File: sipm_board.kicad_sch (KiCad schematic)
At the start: 15 parts, among them Q3 MMBT5088LT1G, Q4 MMBT5088LT1G, U10 MICROFC-60035-SMT-TR1, U9 TPS7B6950DBVR

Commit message: C17,C19,FB1,FB2,FB3 footprint fix
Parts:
- C17, C19: footprint CL21A475KBQNNNE:CAPC2012X140N -> Capacitor_SMD:C_0603_1608Metric; Availability In Stock -> (none); Check_prices https://www.snapeda.com/parts/CL21A475KBQNNNE/Samsung/view-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 -> https://www.snapeda.com/parts/CL10A225KB8NNNC/Samsung%20Ele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; Description_1 CL21 Series 4.7 uF 50 V ±10 % Tolerance X5R SMT Multilayer 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 -> Multilayer Ceramic Capacitors MLCC - SMD/SMT 2.2uF+/-10% 50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; Package 0805 Samsung -> 0603; SnapEDA_Link https://www.snapeda.com/parts/CL21A475KBQNNNE/Samsung/view-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 -> https://www.snapeda.com/parts/CL10A225KB8NNNC/Samsung%20Ele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
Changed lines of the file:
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@@
+	)
+	(symbol
+		(lib_id "CL21A475KBQNNNE:CL21A475KBQNNNE")
+		(at 146.05 101.6 90)
+		(unit 1)
+		(exclude_from_sim no)
+		(in_bom yes)
+		(on_board yes)
+		(dnp no)
+		(property "Reference" "C19"
+			(at 139.7 98.552 90)
+			(effects
+				(font
+					(size 1.27 1.27)
+				)
+				(justify right)
+			)
+		)
+		(property "Value" "2.2u"
+			(at 139.7 101.092 90)
+			(effects
+				(font
+					(size 1.27 1.27)
+				)
+				(justify right)
+			)
+		)
+		(property "Footprint" "Capacitor_SMD:C_0603_1608Metric"
+			(at 146.05 101.6 0)
+			(effects
+				(font
+					(size 1.27 1.27)
+				)
+				(justify bottom)
+				(hide yes)
+			)
+		)
+		(property "Datasheet" ""
+			(at 146.05 101.6 0)
+			(effects
+				(font
+					(size 1.27 1.27)
+				)
+				(hide yes)
+			)
+		)
+		(property "Description" ""
+			(at 146.05 101.6 0)
+			(effects
+				(font
+					(size 1.27 1.27)
+				)
+				(hide yes)
+			)
+		)
+		(property "MF" "Samsung Electro-Mechanics"
+			(at 146.05 101.6 0)
+			(effects
+				(font
+					(size 1.27 1.27)
+				)
+				(justify bottom)
+				(hide yes)
+			)
+		)
+		(property "Description_1" "Multilayer Ceramic Capacitors MLCC - SMD/SMT 2.2uF+/-10% 50V X5R 1608 "
+			(at 146.05 101.6 0)
+			(effects
+				(font
+					(size 1.27 1.27)
+				)
+				(justify bottom)
+				(hide yes)
+			)
+		)
+		(property "Package" "0603"
+			(at 146.05 101.6 0)
+			(effects
+				(font
+					(size 1.27 1.27)
+				)
+				(justify bottom)
+				(hide yes)
+			)
+		)
+		(property "Price" "None"
+			(at 146.05 101.6 0)
+			(effects
+				(font
+					(size 1.27 1.27)
+				)
+				(justify bottom)
+				(hide yes)
+			)
+		)
+		(property "SnapEDA_Link" "https://www.snapeda.com/parts/CL10A225KB8NNNC/Samsung%20Electro-Mechanics/datasheet/"
+			(at 146.05 101.6 0)
+			(effects
+				(font
+					(size 1.27 1.27)
+				)
+				(justify bottom)
+				(hide yes)
+			)
+		)
+		(property "MP" "CL10A225KB8NNNC"
+			(at 146.05 101.6 0)
+			(effects
+				(font
+					(size 1.27 1.27)
+				)
+				(justify bottom)
+				(hide yes)
+			)
+		)
+		(property "Availability" ""
+			(at 146.05 101.6 0)
+			(effects
+				(font
+					(size 1.27 1.27)
+				)
+				(justify bottom)
+				(hide yes)
+			)
+		)
+		(property "Check_prices" "https://www.snapeda.com/parts/CL10A225KB8NNNC/Samsung%20Electro-Mechanics/datasheet/"
+			(at 146.05 101.6 0)
+			(effects
+				(font
+					(size 1.27 1.27)
+				)
+				(justify bottom)
+				(hide yes)
+			)
+		)
+		(pin "1"
+		)
+		(pin "2"
+		)
+		(instances
+			(project "gamma-spectrometer"
+				(path "/1fc9c372-472b-46ca-8d3b-f4aefe31a8be/1929b78d-718a-49ce-a44a-01f5c50b8f35"
+					(reference "C19")
+					(unit 1)
+				)
+			)
+		)
 	)
 	(symbol
@@
 			)
 		)
-		(property "Footprint" "CL21A475KBQNNNE:CAPC2012X140N"
+		(property "Footprint" "Capacitor_SMD:C_0603_1608Metric"
 			(at 100.33 101.6 0)
 			(effects
@@
 			)
 		)
-		(property "Description_1" "\n                        \n                            CL21 Series 4.7 uF 50 V ±10 % Tolerance X5R SMT Multilayer Ceramic Capacitor\n                        \n"
+		(property "Description_1" "Multilayer Ceramic Capacitors MLCC - SMD/SMT 2.2uF+/-10% 50V X5R 1608 "
 			(at 100.33 101.6 0)
 			(effects
@@
 			)
 		)
-		(property "Package" "0805 Samsung"
+		(property "Package" "0603"
 			(at 100.33 101.6 0)
 			(effects
@@
 			)
 		)
-		(property "SnapEDA_Link" "https://www.snapeda.com/parts/CL21A475KBQNNNE/Samsung/view-part/?ref=snap"
+		(property "SnapEDA_Link" "https://www.snapeda.com/parts/CL10A225KB8NNNC/Samsung%20Electro-Mechanics/datasheet/"
 			(at 100.33 101.6 0)
 			(effects
@@
 			)
 		)
-		(property "Availability" "In Stock"
+		(property "Availability" ""
 			(at 100.33 101.6 0)
 			(effects
@@
 			)
 		)
-		(property "Check_prices" "https://www.snapeda.com/parts/CL21A475KBQNNNE/Samsung/view-part/?ref=eda"
+		(property "Check_prices" "https://www.snapeda.com/parts/CL10A225KB8NNNC/Samsung%20Electro-Mechanics/datasheet/"
 			(at 100.33 101.6 0)
 			(effects
@@
 					(unit 1)
 				)
-			)
-		)
-	)
-	(symbol
-		(lib_id "CL21A475KBQNNNE:CL21A475KBQNNNE")
-		(at 146.05 101.6 90)
-		(unit 1)
-		(exclude_from_sim no)
-		(in_bom yes)
-		(on_board yes)
-		(dnp no)
-		(property "Reference" "C19"
-			(at 139.7 98.552 90)
-			(effects
-				(font
-					(size 1.27 1.27)
-				)
-				(justify right)
-			)
-		)
-		(property "Value" "2.2u"
-			(at 139.7 101.092 90)
-			(effects
-				(font
-					(size 1.27 1.27)
-				)
-				(justify right)
-			)
-		)
-		(property "Footprint" "CL21A475KBQNNNE:CAPC2012X140N"
-			(at 146.05 101.6 0)
-			(effects
-				(font
-					(size 1.27 1.27)
-				)
-				(justify bottom)
-				(hide yes)
-			)
-		)
-		(property "Datasheet" ""
-			(at 146.05 101.6 0)
-			(effects
-				(font
-					(size 1.27 1.27)
-				)
-				(hide yes)
-			)
-		)
-		(property "Description" ""
-			(at 146.05 101.6 0)
-			(effects
-				(font
-					(size 1.27 1.27)
-				)
-				(hide yes)
-			)
-		)
-		(property "MF" "Samsung Electro-Mechanics"
-			(at 146.05 101.6 0)
-			(effects
-				(font
-					(size 1.27 1.27)
-				)
-				(justify bottom)
-				(hide yes)
-			)
-		)
-		(property "Description_1" "\n                        \n                            CL21 Series 4.7 uF 50 V ±10 % Tolerance X5R SMT Multilayer Ceramic Capacitor\n                        \n"
-			(at 146.05 101.6 0)
-			(effects
-				(font
-					(size 1.27 1.27)
-				)
-				(justify bottom)
-				(hide yes)
-			)
-		)
-		(property "Package" "0805 Samsung"
-			(at 146.05 101.6 0)
-			(effects
-				(font
-					(size 1.27 1.27)
-				)
-				(justify bottom)
-				(hide yes)
-			)
-		)
-		(property "Price" "None"
-			(at 146.05 101.6 0)
-			(effects
-				(font
-					(size 1.27 1.27)
-				)
-				(justify bottom)
-				(hide yes)
-			)
-		)
-		(property "SnapEDA_Link" "https://www.snapeda.com/parts/CL21A475KBQNNNE/Samsung/view-part/?ref=snap"
-			(at 146.05 101.6 0)
-			(effects
-				(font
-					(size 1.27 1.27)
-				)
-				(justify bottom)
-				(hide yes)
-			)
-		)
-		(property "MP" "CL10A225KB8NNNC"
-			(at 146.05 101.6 0)
-			(effects
-				(font
-					(size 1.27 1.27)
-				)
-				(justify bottom)
-				(hide yes)
-			)
-		)
-		(property "Availability" "In Stock"
-			(at 146.05 101.6 0)
-			(effects
-				(font
-					(size 1.27 1.27)
-				)
-				(justify bottom)
-				(hide yes)
-			)
-		)
-		(property "Check_prices" "https://www.snapeda.com/parts/CL21A475KBQNNNE/Samsung/view-part/?ref=eda"
-			(at 146.05 101.6 0)
-			(effects
-				(font
-					(size 1.27 1.27)
-				)
-				(justify bottom)
-				(hide yes)
-			)
-		)
-		(pin "1"
-		)
-		(pin "2"
-		)
-		(instances
-			(project "gamma-spectrometer"
-				(path "/1fc9c372-472b-46ca-8d3b-f4aefe31a8be/1929b78d-718a-49ce-a44a-01f5c50b8f35"
-					(reference "C19")
-					(unit 1)
-				)

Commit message: Updated 3d models
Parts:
- renumbered U9 to U5, U10 to U6
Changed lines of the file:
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@@
 		(on_board yes)
 		(dnp no)
-		(property "Reference" "U10"
+		(property "Reference" "U6"
 			(at 210.566 72.136 90)
 			(effects
@@
 			(project ""
 				(path "/1fc9c372-472b-46ca-8d3b-f4aefe31a8be/1929b78d-718a-49ce-a44a-01f5c50b8f35"
-					(reference "U10")
+					(reference "U6")
 					(unit 1)
 				)
@@
 		(on_board yes)
 		(dnp no)
-		(property "Reference" "U9"
+		(property "Reference" "U5"
 			(at 121.92 85.852 0)
 			(effects
@@
 			(project ""
 				(path "/1fc9c372-472b-46ca-8d3b-f4aefe31a8be/1929b78d-718a-49ce-a44a-01f5c50b8f35"
-					(reference "U9")
+					(reference "U5")
 					(unit 1)
 				)

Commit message: MCP41050 replaces pot for SiPM PS regulation
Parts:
- renumbered U6 to U7
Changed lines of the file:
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@@
 		(on_board yes)
 		(dnp no)
-		(property "Reference" "U6"
+		(property "Reference" "U7"
 			(at 210.566 72.136 90)
 			(effects
@@
 			(project ""
 				(path "/1fc9c372-472b-46ca-8d3b-f4aefe31a8be/1929b78d-718a-49ce-a44a-01f5c50b8f35"
-					(reference "U6")
+					(reference "U7")
 					(unit 1)
 				)

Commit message: ADC capacitors
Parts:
- renumbered C17 to C24, C19 to C25, C20 to C26, C21 to C27, C22 to C28, Q3 to Q1, Q4 to Q2

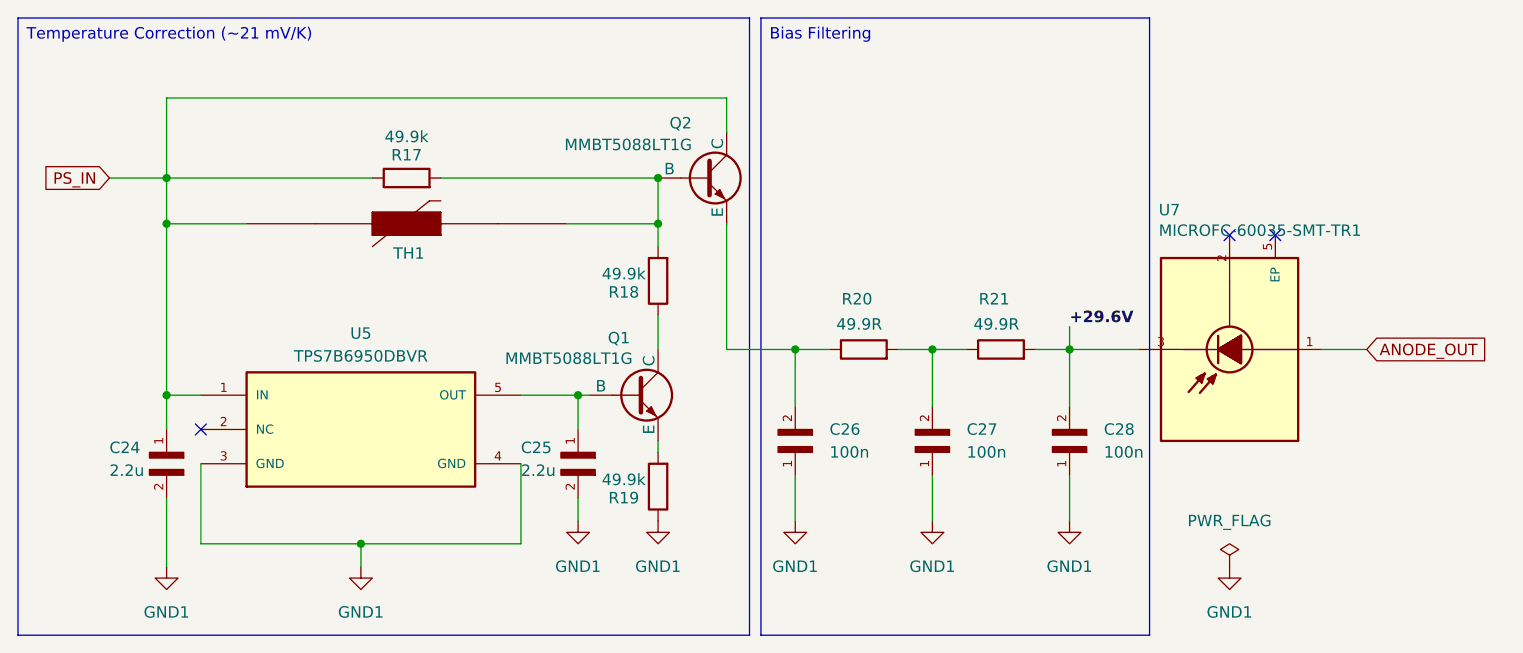
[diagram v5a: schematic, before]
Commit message: Digital potentiometer improvement
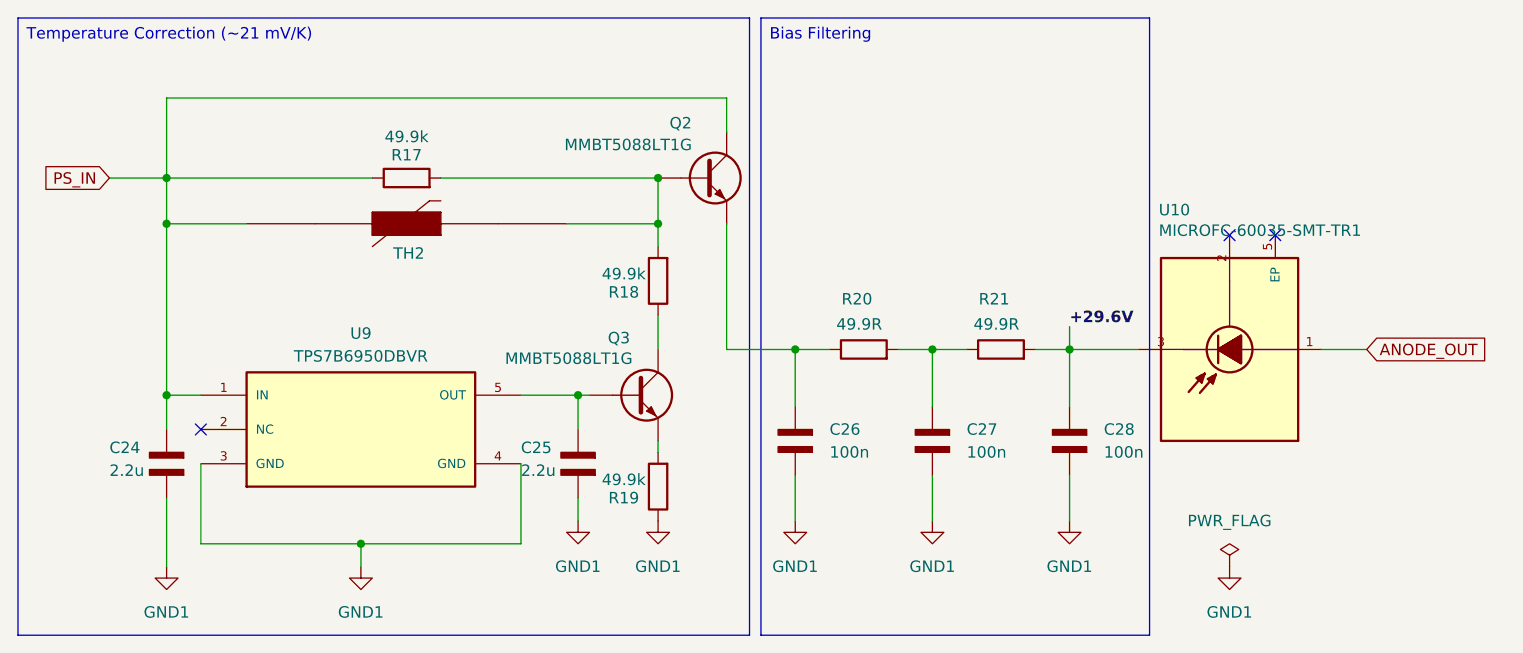
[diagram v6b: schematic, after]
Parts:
- renumbered Q1 to Q3, TH1 to TH2, U7 to U10, U5 to U9
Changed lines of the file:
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@@
 	(title_block
 		(title "SiPM Board")
-		(date "2025-06-04")
-		(rev "0.2.0")
+		(date "2025-09-06")
+		(rev "0.2.1")
 		(company "Vadym Vikulin")
 		(comment 7 "Temperature Correction (~21 mV/K)")
@@
 	)
 	(symbol
+		(lib_name "CL21A475KBQNNNE_1")
 		(lib_id "CL21A475KBQNNNE:CL21A475KBQNNNE")
 		(at 146.05 101.6 90)
@@
 	)
 	(symbol
+		(lib_name "NPN_1")
 		(lib_id "Simulation_SPICE:NPN")
 		(at 152.4 92.71 0)
@@
 		(on_board yes)
 		(dnp no)
-		(property "Reference" "Q1"
+		(property "Reference" "Q3"
 			(at 149.352 86.36 0)
 			(effects
@@
 			(project ""
 				(path "/1fc9c372-472b-46ca-8d3b-f4aefe31a8be/1929b78d-718a-49ce-a44a-01f5c50b8f35"
-					(reference "Q1")
+					(reference "Q3")
 					(unit 1)
 				)
@@
 		(dnp no)
 		(fields_autoplaced yes)
-		(property "Reference" "#PWR064"
+		(property "Reference" "#PWR025"
 			(at 121.92 118.11 0)
 			(effects
@@
 			(project ""
 				(path "/1fc9c372-472b-46ca-8d3b-f4aefe31a8be/1929b78d-718a-49ce-a44a-01f5c50b8f35"
-					(reference "#PWR064")
+					(reference "#PWR025")
 					(unit 1)
 				)
@@
 		(on_board yes)
 		(dnp no)
-		(property "Reference" "TH1"
+		(property "Reference" "TH2"
 			(at 127.254 76.962 0)
 			(effects
@@
 		(pin "2"
 		)
-		(instances
-			(project ""
-				(path "/1fc9c372-472b-46ca-8d3b-f4aefe31a8be/1929b78d-718a-49ce-a44a-01f5c50b8f35"
-					(reference "TH1")
-					(unit 1)
-				)
-			)
-		)
 	)
 	(symbol
@@
 		(on_board yes)
 		(dnp no)
-		(property "Reference" "U7"
+		(property "Reference" "U10"
 			(at 210.566 72.136 90)
 			(effects
@@
 		(pin "5"
 		)
-		(instances
-			(project ""
-				(path "/1fc9c372-472b-46ca-8d3b-f4aefe31a8be/1929b78d-718a-49ce-a44a-01f5c50b8f35"
-					(reference "U7")
-					(unit 1)
-				)
-			)
-		)
 	)
 	(symbol
@@
 	)
 	(symbol
+		(lib_name "CL10B104KC8NNNC_1")
 		(lib_id "CL10B104KC8NNNC:CL10B104KC8NNNC")
 		(at 170.18 99.06 90)
@@
 		(on_board yes)
 		(dnp no)
-		(property "Reference" "U5"
+		(property "Reference" "U9"
 			(at 121.92 85.852 0)
 			(effects
@@
 		(pin "5"
 		)
-		(instances
-			(project ""
-				(path "/1fc9c372-472b-46ca-8d3b-f4aefe31a8be/1929b78d-718a-49ce-a44a-01f5c50b8f35"
-					(reference "U5")
-					(unit 1)
-				)
-			)
-		)
 	)
 	(symbol
@@
 	)
 	(symbol
+		(lib_name "CL10B104KC8NNNC_2")
 		(lib_id "CL10B104KC8NNNC:CL10B104KC8NNNC")
 		(at 185.42 99.06 90)

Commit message: 3d models update
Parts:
- renumbered TH2 to TH1
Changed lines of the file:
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@@
 		(on_board yes)
 		(dnp no)
-		(property "Reference" "TH2"
+		(property "Reference" "TH1"
 			(at 127.254 76.962 0)
 			(effects
@@
 		)
 		(pin "2"
+		)
+		(instances
+			(project "gamma-spectrometer"
+				(path "/1fc9c372-472b-46ca-8d3b-f4aefe31a8be/1929b78d-718a-49ce-a44a-01f5c50b8f35"
+					(reference "TH1")
+					(unit 1)
+				)
+			)
 		)
 	)
@@
 		)
 		(pin "5"
+		)
+		(instances
+			(project "gamma-spectrometer"
+				(path "/1fc9c372-472b-46ca-8d3b-f4aefe31a8be/1929b78d-718a-49ce-a44a-01f5c50b8f35"
+					(reference "U10")
+					(unit 1)
+				)
+			)
 		)
 	)
@@
 		(pin "5"
 		)
+		(instances
+			(project "gamma-spectrometer"
+				(path "/1fc9c372-472b-46ca-8d3b-f4aefe31a8be/1929b78d-718a-49ce-a44a-01f5c50b8f35"
+					(reference "U9")
+					(unit 1)
+				)
+			)
+		)
 	)
